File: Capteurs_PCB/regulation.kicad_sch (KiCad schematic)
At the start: 23 parts, among them U2 AZ1117-3.3

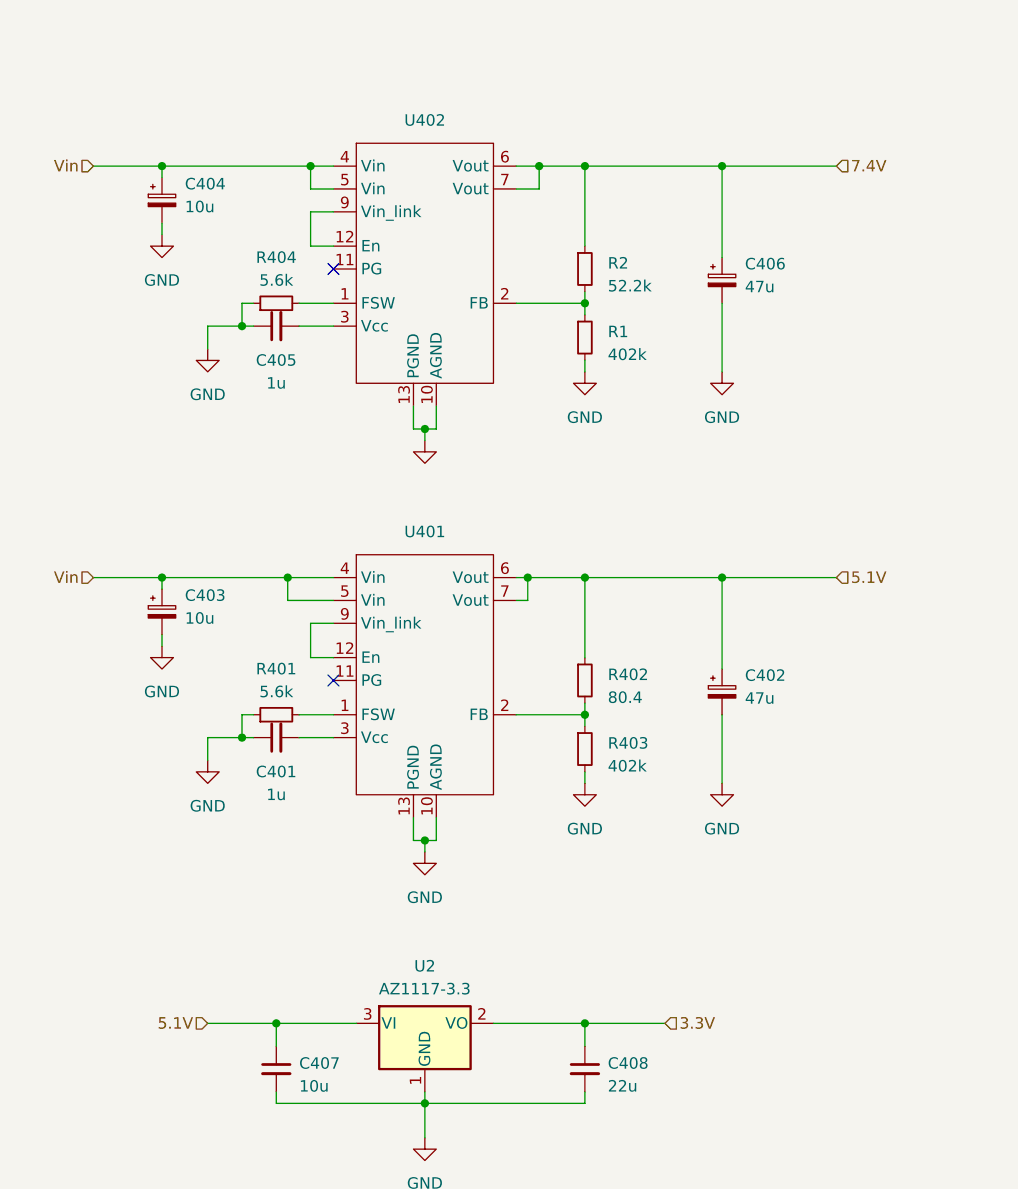
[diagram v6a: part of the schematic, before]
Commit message: ST-LINK sur Kicad
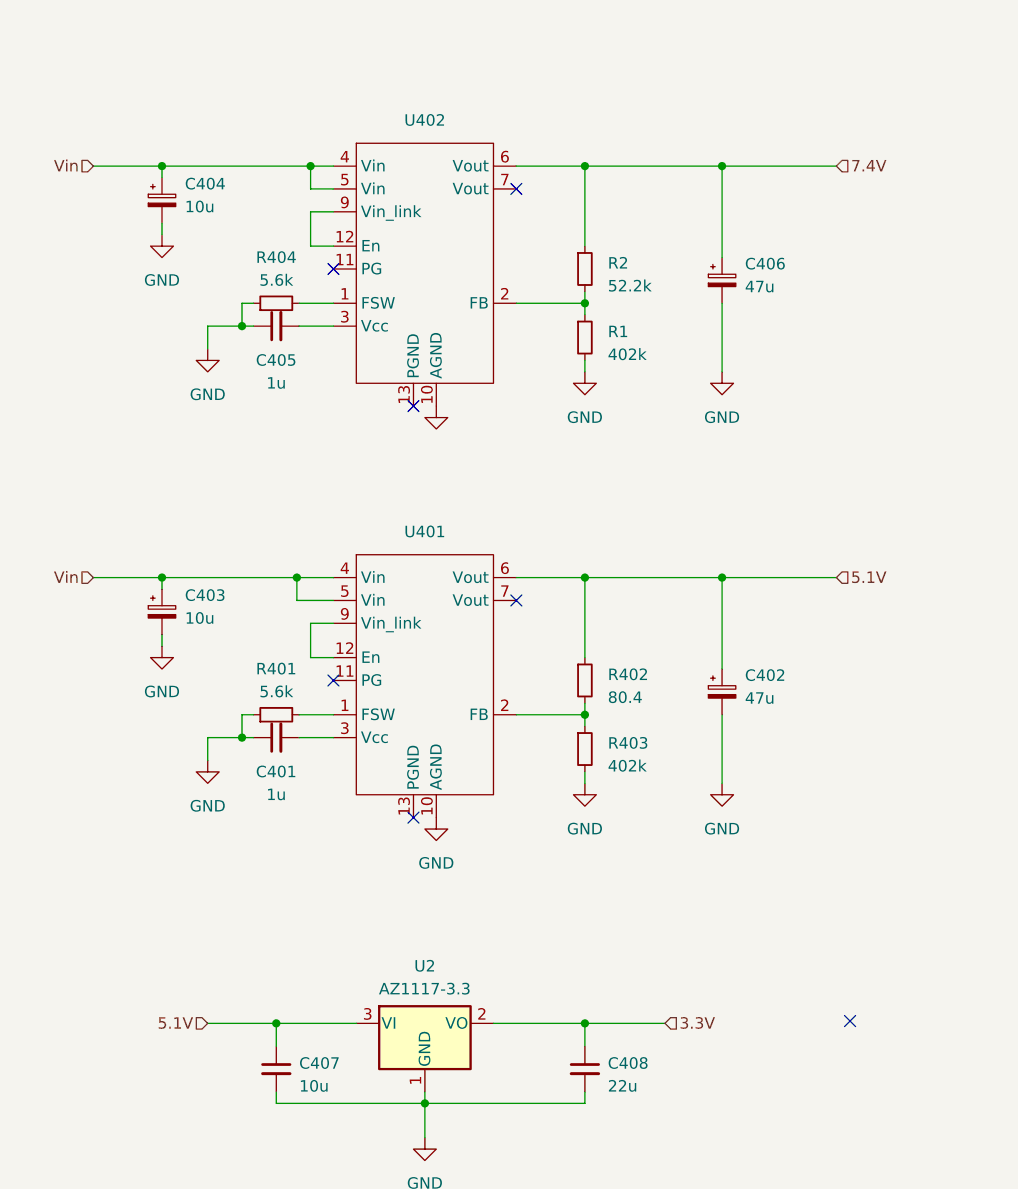
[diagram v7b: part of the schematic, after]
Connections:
- net 5.1V: no longer U401.7 (Vout)
- net 7.4V: no longer U402.7 (Vout)
- net GND: no longer U401.13 (PGND), U402.13 (PGND)
- no-connect marks 2 -> 7
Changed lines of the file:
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@@
   (junction (at 86.36 156.21) (diameter 0) (color 0 0 0 0)
   )
-  (junction (at 86.36 81.28) (diameter 0) (color 0 0 0 0)
+  (junction (at 72.136 97.79) (diameter 0) (color 0 0 0 0)
   )
   (junction (at 57.15 52.07) (diameter 0) (color 0 0 0 0)
@@
   (junction (at 66.04 69.85) (diameter 0) (color 0 0 0 0)
   )
-  (junction (at 97.79 97.79) (diameter 0) (color 0 0 0 0)
-  )
   (junction (at 104.14 113.03) (diameter 0) (color 0 0 0 0)
   )
   (junction (at 66.04 115.57) (diameter 0) (color 0 0 0 0)
   )
-  (junction (at 86.36 127) (diameter 0) (color 0 0 0 0)
-  )
   (junction (at 73.66 52.07) (diameter 0) (color 0 0 0 0)
   )
@@
   (junction (at 69.85 147.32) (diameter 0) (color 0 0 0 0)
   )
-  (junction (at 99.06 52.07) (diameter 0) (color 0 0 0 0)
-  )
-  (junction (at 71.12 97.79) (diameter 0) (color 0 0 0 0)
-  )
+  (no_connect (at 85.09 124.46))
+  (no_connect (at 96.52 100.33))
+  (no_connect (at 133.604 147.066))
   (no_connect (at 76.2 63.5))
+  (no_connect (at 96.52 54.61))
+  (no_connect (at 85.09 78.74))
   (no_connect (at 76.2 109.22))
   (wire (pts (xy 185.42 76.2) (xy 185.42 78.74))
@@
     (stroke (width 0) (type default))
   )
-  (wire (pts (xy 97.79 100.33) (xy 97.79 97.79))
-    (stroke (width 0) (type default))
-  )
   (wire (pts (xy 76.2 54.61) (xy 73.66 54.61))
     (stroke (width 0) (type default))
@@
     (stroke (width 0) (type default))
   )
-  (wire (pts (xy 57.15 97.79) (xy 71.12 97.79))
-    (stroke (width 0) (type default))
-  )
   (wire (pts (xy 104.14 111.76) (xy 104.14 113.03))
     (stroke (width 0) (type default))
@@
     (stroke (width 0) (type default))
   )
-  (wire (pts (xy 96.52 100.33) (xy 97.79 100.33))
-    (stroke (width 0) (type default))
-  )
   (wire (pts (xy 104.14 154.94) (xy 104.14 156.21))
     (stroke (width 0) (type default))
@@
     (stroke (width 0) (type default))
   )
-  (wire (pts (xy 99.06 52.07) (xy 104.14 52.07))
-    (stroke (width 0) (type default))
-  )
-  (wire (pts (xy 96.52 52.07) (xy 99.06 52.07))
+  (wire (pts (xy 96.52 52.07) (xy 104.14 52.07))
     (stroke (width 0) (type default))
   )
@@
     (stroke (width 0) (type default))
   )
-  (wire (pts (xy 97.79 97.79) (xy 96.52 97.79))
-    (stroke (width 0) (type default))
-  )
   (wire (pts (xy 66.04 69.85) (xy 66.04 67.31))
     (stroke (width 0) (type default))
@@
     (stroke (width 0) (type default))
   )
-  (wire (pts (xy 86.36 81.28) (xy 87.63 81.28))
-    (stroke (width 0) (type default))
-  )
-  (wire (pts (xy 99.06 54.61) (xy 99.06 52.07))
-    (stroke (width 0) (type default))
-  )
   (wire (pts (xy 86.36 154.94) (xy 86.36 156.21))
     (stroke (width 0) (type default))
@@
     (stroke (width 0) (type default))
   )
+  (wire (pts (xy 72.136 97.79) (xy 76.2 97.79))
+    (stroke (width 0) (type default))
+  )
   (wire (pts (xy 57.15 104.14) (xy 57.15 105.41))
     (stroke (width 0) (type default))
@@
     (stroke (width 0) (type default))
   )
-  (wire (pts (xy 87.63 124.46) (xy 87.63 127))
-    (stroke (width 0) (type default))
-  )
   (wire (pts (xy 104.14 97.79) (xy 104.14 106.68))
     (stroke (width 0) (type default))
   )
-  (wire (pts (xy 87.63 78.74) (xy 87.63 81.28))
-    (stroke (width 0) (type default))
-  )
   (wire (pts (xy 72.39 67.31) (xy 76.2 67.31))
     (stroke (width 0) (type default))
   )
-  (wire (pts (xy 96.52 54.61) (xy 99.06 54.61))
-    (stroke (width 0) (type default))
-  )
   (wire (pts (xy 62.23 69.85) (xy 66.04 69.85))
     (stroke (width 0) (type default))
   )
-  (wire (pts (xy 86.36 127) (xy 86.36 128.27))
-    (stroke (width 0) (type default))
-  )
   (wire (pts (xy 62.23 115.57) (xy 66.04 115.57))
     (stroke (width 0) (type default))
@@
     (stroke (width 0) (type default))
   )
+  (wire (pts (xy 76.2 100.33) (xy 72.136 100.33))
+    (stroke (width 0) (type default))
+  )
   (wire (pts (xy 104.14 66.04) (xy 104.14 67.31))
     (stroke (width 0) (type default))
   )
-  (wire (pts (xy 86.36 81.28) (xy 86.36 82.55))
-    (stroke (width 0) (type default))
-  )
   (wire (pts (xy 67.31 115.57) (xy 66.04 115.57))
     (stroke (width 0) (type default))
@@
     (stroke (width 0) (type default))
   )
-  (wire (pts (xy 71.12 100.33) (xy 76.2 100.33))
-    (stroke (width 0) (type default))
-  )
-  (wire (pts (xy 76.2 97.79) (xy 71.12 97.79))
-    (stroke (width 0) (type default))
-  )
-  (wire (pts (xy 86.36 127) (xy 87.63 127))
-    (stroke (width 0) (type default))
-  )
-  (wire (pts (xy 85.09 127) (xy 86.36 127))
+  (wire (pts (xy 57.15 97.79) (xy 72.136 97.79))
     (stroke (width 0) (type default))
   )
@@
     (stroke (width 0) (type default))
   )
+  (wire (pts (xy 72.136 100.33) (xy 72.136 97.79))
+    (stroke (width 0) (type default))
+  )
   (wire (pts (xy 72.39 115.57) (xy 76.2 115.57))
     (stroke (width 0) (type default))
@@
     (stroke (width 0) (type default))
   )
-  (wire (pts (xy 85.09 81.28) (xy 86.36 81.28))
-    (stroke (width 0) (type default))
-  )
   (wire (pts (xy 86.36 156.21) (xy 104.14 156.21))
     (stroke (width 0) (type default))
@@
     (stroke (width 0) (type default))
   )
-  (wire (pts (xy 85.09 78.74) (xy 85.09 81.28))
-    (stroke (width 0) (type default))
-  )
   (wire (pts (xy 213.36 64.77) (xy 213.36 71.12))
     (stroke (width 0) (type default))
   )
-  (wire (pts (xy 85.09 124.46) (xy 85.09 127))
-    (stroke (width 0) (type default))
-  )
   (wire (pts (xy 76.2 102.87) (xy 73.66 102.87))
     (stroke (width 0) (type default))
   )
-  (wire (pts (xy 97.79 97.79) (xy 104.14 97.79))
-    (stroke (width 0) (type default))
-  )
-  (wire (pts (xy 71.12 97.79) (xy 71.12 100.33))
+  (wire (pts (xy 96.52 97.79) (xy 104.14 97.79))
     (stroke (width 0) (type default))
   )
@@
     )
   )
+  (symbol (lib_id "power:GND") (at 87.63 78.74 0) (unit 1)
+    (in_bom yes) (on_board yes) (dnp no) (fields_autoplaced)
+    (property "Reference" "#PWR030" (at 87.63 85.09 0)
+      (effects (font (size 1.27 1.27)) hide)
+    )
+    (property "Value" "GND" (at 87.63 83.82 0)
+      (effects (font (size 1.27 1.27)) hide)
+    )
+    (property "Footprint" "" (at 87.63 78.74 0)
+      (effects (font (size 1.27 1.27)) hide)
+    )
+    (property "Datasheet" "" (at 87.63 78.74 0)
+      (effects (font (size 1.27 1.27)) hide)
+    )
+    (pin "1")
+    (instances
+      (project "Capteurs_PCB"
+        (path "/1101af8f-9425-4102-9245-339dc54562bf/b84a61ef-89d4-47b7-a16e-5e36daa53b0c"
+          (reference "#PWR030") (unit 1)
+        )
+      )
+    )
+  )
   (symbol (lib_id "Device:C_Small") (at 104.14 152.4 0) (unit 1)
     (in_bom yes) (on_board yes) (dnp no) (fields_autoplaced)
@@
         (path "/1101af8f-9425-4102-9245-339dc54562bf/b84a61ef-89d4-47b7-a16e-5e36daa53b0c"
           (reference "R404") (unit 1)
-        )
-      )
-    )
-  )
-  (symbol (lib_id "power:GND") (at 86.36 82.55 0) (unit 1)
-    (in_bom yes) (on_board yes) (dnp no) (fields_autoplaced)
-    (property "Reference" "#PWR0408" (at 86.36 88.9 0)
-      (effects (font (size 1.27 1.27)) hide)
-    )
-    (property "Value" "GND" (at 86.36 87.63 0)
-      (effects (font (size 1.27 1.27)) hide)
-    )
-    (property "Footprint" "" (at 86.36 82.55 0)
-      (effects (font (size 1.27 1.27)) hide)
-    )
-    (property "Datasheet" "" (at 86.36 82.55 0)
-      (effects (font (size 1.27 1.27)) hide)
-    )
-    (pin "1")
-    (instances
-      (project "Capteurs_PCB"
-        (path "/1101af8f-9425-4102-9245-339dc54562bf/b84a61ef-89d4-47b7-a16e-5e36daa53b0c"
-          (reference "#PWR0408") (unit 1)
         )
       )
@@
     )
   )
-  (symbol (lib_id "power:GND") (at 86.36 128.27 0) (unit 1)
-    (in_bom yes) (on_board yes) (dnp no) (fields_autoplaced)
-    (property "Reference" "#PWR0401" (at 86.36 134.62 0)
-      (effects (font (size 1.27 1.27)) hide)
-    )
-    (property "Value" "GND" (at 86.36 133.35 0)
-      (effects (font (size 1.27 1.27)))
-    )
-    (property "Footprint" "" (at 86.36 128.27 0)
-      (effects (font (size 1.27 1.27)) hide)
-    )
-    (property "Datasheet" "" (at 86.36 128.27 0)
-      (effects (font (size 1.27 1.27)) hide)
-    )
+  (symbol (lib_id "power:GND") (at 87.63 124.46 0) (unit 1)
+    (in_bom yes) (on_board yes) (dnp no) (fields_autoplaced)
+    (property "Reference" "#PWR0401" (at 87.63 130.81 0)
+      (effects (font (size 1.27 1.27)) hide)
+    )
+    (property "Value" "GND" (at 87.63 129.54 0)
+      (effects (font (size 1.27 1.27)))
+    )
+    (property "Footprint" "" (at 87.63 124.46 0)
+      (effects (font (size 1.27 1.27)) hide)
+    )
+    (property "Datasheet" "" (at 87.63 124.46 0)
+      (effects (font (size 1.27 1.27)) hide)
+    )

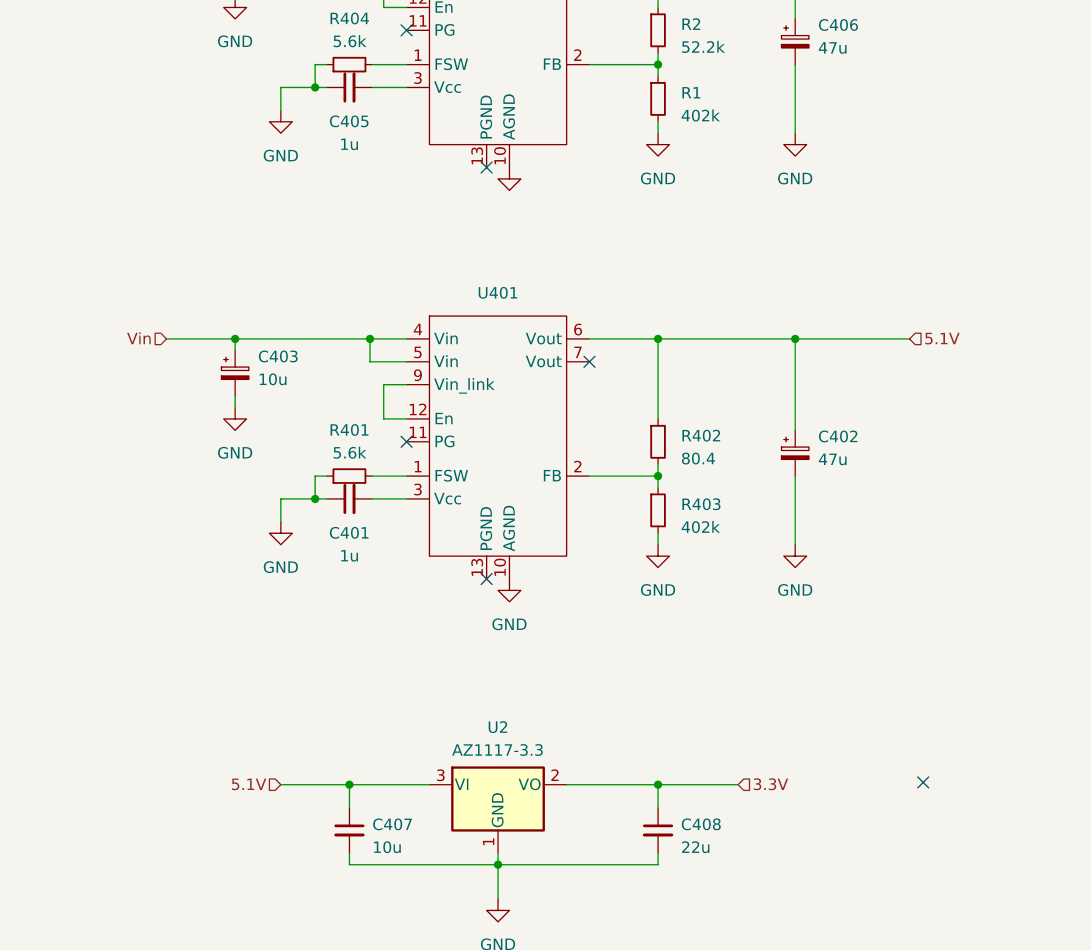
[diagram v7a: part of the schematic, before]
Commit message: Enlever les erreurs Kicad+Mettre connecteur batterie
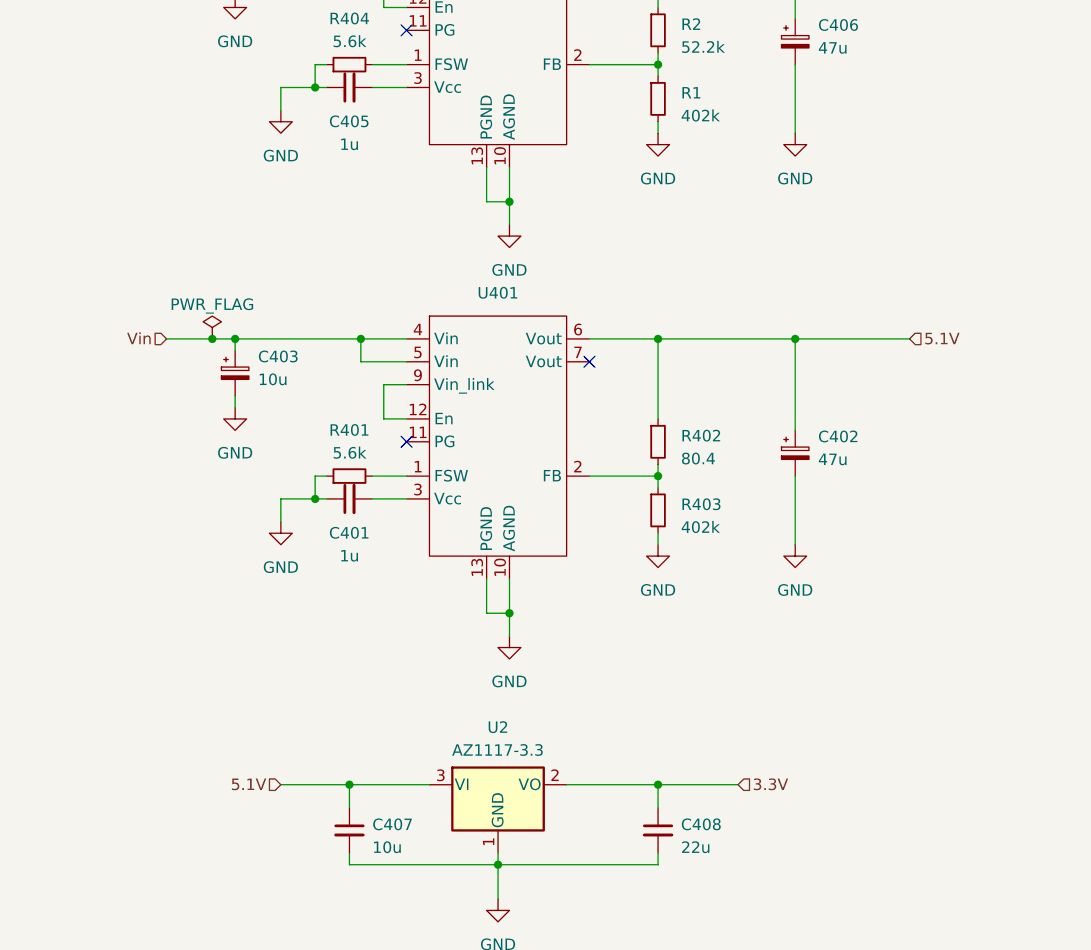
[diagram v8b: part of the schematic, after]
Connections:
- net GND: now also U401.13 (PGND), U402.13 (PGND)
- no-connect marks 7 -> 4
